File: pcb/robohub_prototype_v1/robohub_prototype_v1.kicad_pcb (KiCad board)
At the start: 10 copper layers, 102 parts, among them J21 Barrel_Jack_Switch_Pin3Ring, J51 USB_A, J52 USB_A, J71 USB_A, U1 ATSAMA5D27C, U21 LM3880, U22 TPS564242DRL, U23 TPS564242DRL, U24 TPS564242DRL, U25 TPS564242DRL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

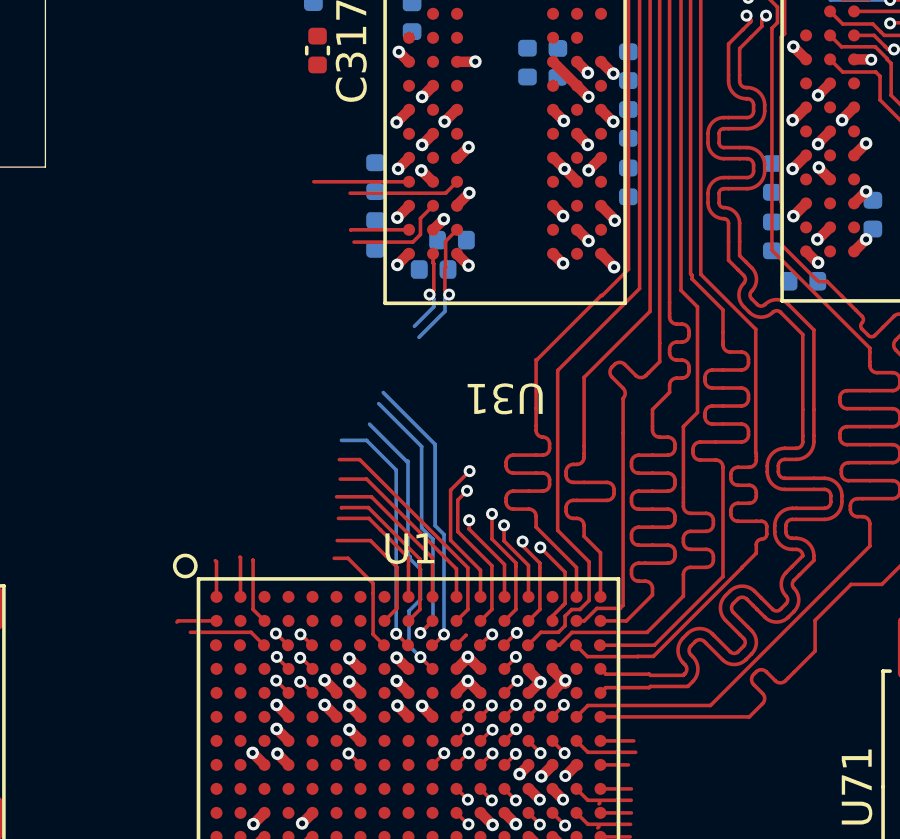
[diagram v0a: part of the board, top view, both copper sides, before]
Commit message: Routing data bytes
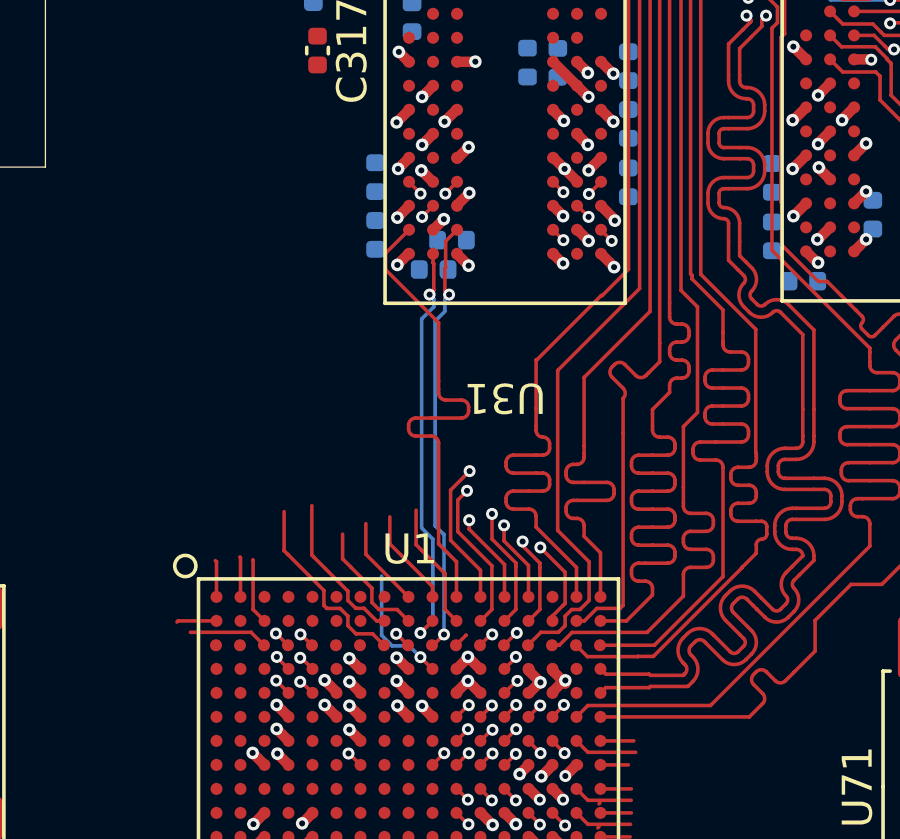
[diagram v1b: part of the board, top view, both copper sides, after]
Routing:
- net /DDR2_3/DDR_D18: track 12.0 -> 1.18 mm, vias 1 -> 2
- net /DDR2_3/DDR_D23: track 8.00 -> 16.9 mm
- net /DDR2_3/DDR_D21: track 12.5 -> 4.69 mm, vias 1 -> 2
- net /DDR2_3/DDR_DQM2: track 3.91 -> 6.90 mm, vias 0 -> 1
- net /DDR2_3/DDR_D22: track 7.73 -> 4.79 mm, vias 0 -> 1
- net /DDR2_3/DDR_D16: track 7.78 -> 5.68 mm, vias 0 -> 1
- net /DDR2_3/DDR_DQS2-: track 12.0 -> 13.9 mm
- net /DDR2_3/DDR_D20: track 5.34 -> 3.83 mm, vias 0 -> 1
- net /DDR2_3/DDR_DQS2+: track 13.7 -> 14.6 mm
- net /DDR2_3/DDR_D17: track 5.58 -> 4.73 mm, vias 0 -> 1
- net /DDR2_3/DDR_D19: track 4.18 -> 3.52 mm, vias 0 -> 1

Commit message: Updates to routing second byte lane
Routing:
- net /DDR2_3/DDR_D18: track 1.18 -> 18.6 mm
- net /DDR2_3/DDR_D16: track 5.68 -> 21.9 mm, vias 1 -> 0
- net /DDR2_3/DDR_D19: track 3.52 -> 18.9 mm
- net /DDR2_3/DDR_D21: track 4.69 -> 19.6 mm
- net /DDR2_3/DDR_D20: track 3.83 -> 18.5 mm, vias 1 -> 2
- net /DDR2_3/DDR_D17: track 4.73 -> 19.3 mm, vias 1 -> 2
- net /DDR2_3/DDR_D22: track 4.79 -> 18.0 mm, vias 1 -> 2
- net /DDR2_3/DDR_DQM2: track 6.90 -> 19.8 mm, vias 1 -> 2
- net /DDR2_3/DDR_RAS: track 37.2 -> 48.9 mm
- net /DDR2_3/DDR_WE: track 43.1 -> 49.5 mm
- net /DDR2_3/DDR_CS: track 41.6 -> 47.8 mm
- net /DDR2_3/DDR_D5: track 0.61 -> 6.42 mm, vias 1 -> 2
- net /DDR2_3/DDR_D2: track 0.61 -> 5.13 mm, vias 1 -> 2
- net /DDR2_3/DDR_A6: track 45.9 -> 49.8 mm
- net /DDR2_3/DDR_DQS2+: track 14.6 -> 18.4 mm
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
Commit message: Rip up to begin reroute
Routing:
- net /DDR2_3/DDR_A11: track 55.9 -> 3.94 mm, vias 2 -> 1
- net /DDR2_3/DDR_CKE: track 56.4 -> 7.86 mm, vias 2 -> 1
- net /DDR2_3/DDR_CLK-: track 55.8 -> 7.91 mm, vias 2 -> 1
- net /DDR2_3/DDR_BA2: track 56.5 -> 8.78 mm, vias 2 -> 1
- net /DDR2_3/DDR_CLK+: track 55.2 -> 7.63 mm, vias 2 -> 1
- net /DDR2_3/DDR_A2: track 49.6 -> 3.30 mm, vias 2 -> 1
- net /DDR2_3/DDR_A7: track 56.3 -> 10.6 mm, vias 2 -> 1
- net /DDR2_3/DDR_A4: track 50.8 -> 6.43 mm, vias 2 -> 1
- net /DDR2_3/DDR_A1: track 48.2 -> 4.70 mm, vias 2 -> 1
- net /DDR2_3/DDR_A12: track 49.3 -> 5.79 mm, vias 2 -> 1
- net /DDR2_3/DDR_A13: track 56.0 -> 13.9 mm, vias 3 -> 2
- net /DDR2_3/DDR_A3: track 49.4 -> 7.28 mm, vias 2 -> 1
- net /DDR2_3/DDR_A8: track 50.9 -> 8.91 mm, vias 2 -> 1
- net /DDR2_3/DDR_A10: track 49.1 -> 7.36 mm, vias 2 -> 1
- net /DDR2_3/DDR_CAS: track 51.0 -> 10.4 mm, vias 3 -> 2
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
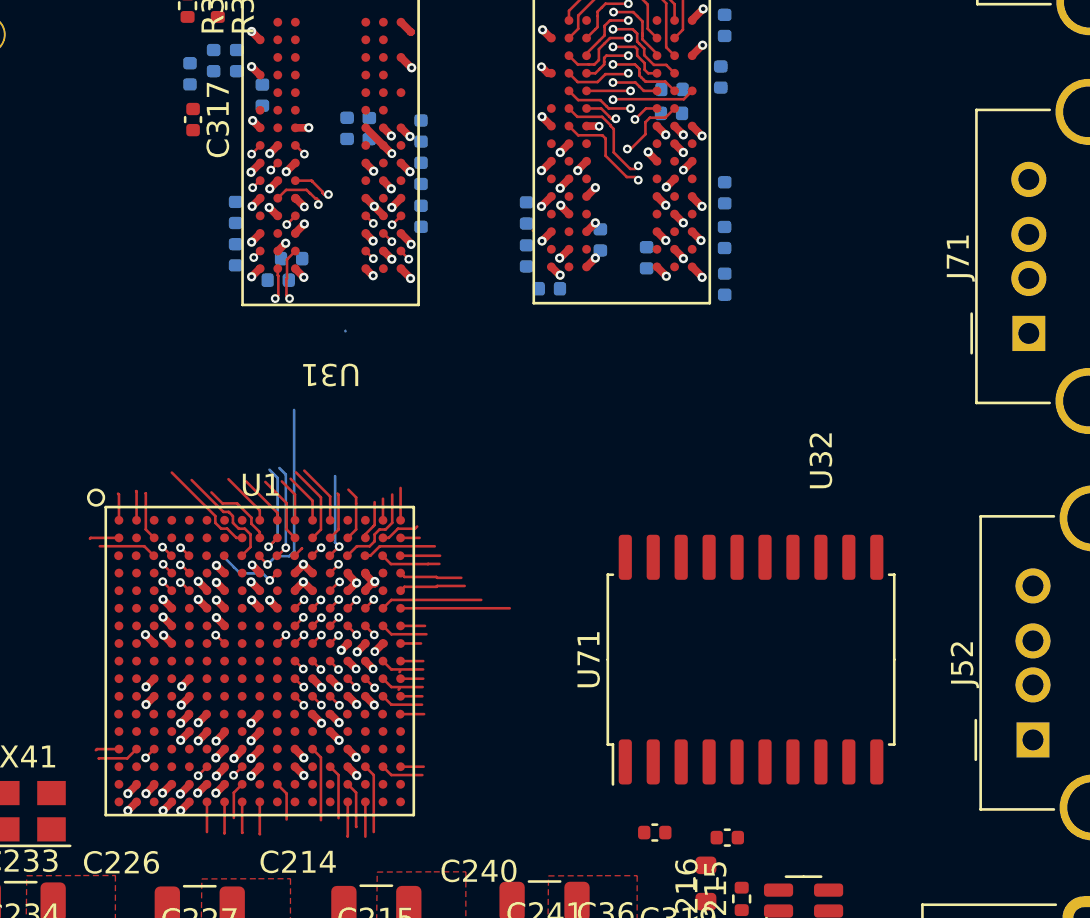
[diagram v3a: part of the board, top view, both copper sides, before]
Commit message: Routed 3/4 data bytes, no length matching
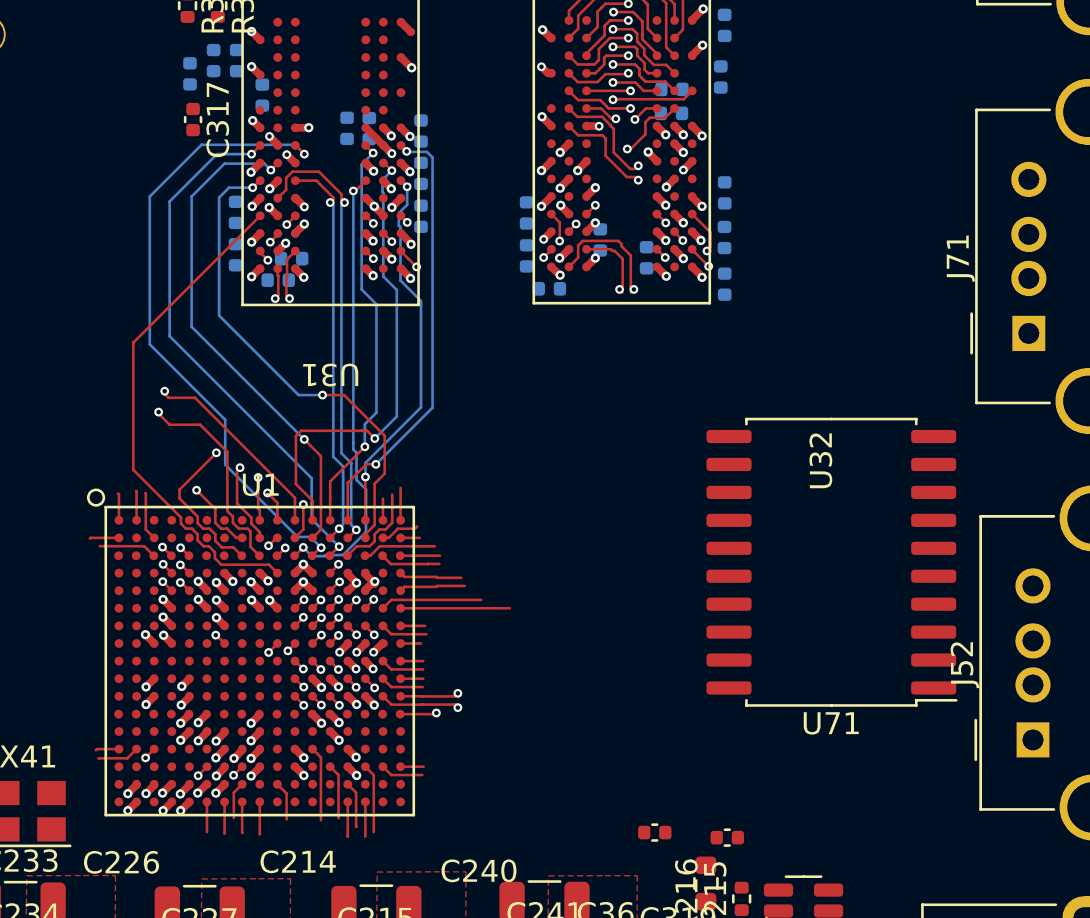
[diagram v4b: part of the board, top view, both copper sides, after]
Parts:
- moved U71 5.74 mm to (147.8, 90.2), turned to 180 degrees
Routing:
- net /DDR2_3/DDR_D27: track 0.58 -> 45.9 mm, vias 1 -> 2
- net /DDR2_3/DDR_D30: track 0.59 -> 38.9 mm, vias 1 -> 2
- net /DDR2_3/DDR_D28: track 0.66 -> 38.6 mm, vias 1 -> 2
- net /DDR2_3/DDR_D25: track 0.55 -> 37.7 mm, vias 1 -> 2
- net /DDR2_3/DDR_DQM3: track 0.69 -> 34.7 mm, vias 1 -> 2
- net /DDR2_3/DDR_DQS3-: track 1.93 -> 35.4 mm, vias 0 -> 2
- net /DDR2_3/DDR_D29: track 0.63 -> 33.8 mm, vias 1 -> 2
- net /DDR2_3/DDR_D26: track 0.53 -> 32.8 mm, vias 1 -> 2
- net /DDR2_3/DDR_D24: track 0.54 -> 32.0 mm, vias 1 -> 2
- net /DDR2_3/DDR_DQS3+: track 0.99 -> 31.5 mm, vias 0 -> 2
- net /DDR2_3/DDR_D31: track 1.09 -> 29.0 mm, vias 0 -> 2
- net /DDR2_3/DDR_D2: track 5.13 -> 29.5 mm
- net /DDR2_3/DDR_DQM0: track 0.47 -> 20.5 mm, vias 0 -> 2
- net /DDR2_3/DDR_D4: track 0.00 -> 20.0 mm, vias 0 -> 2
- net /DDR2_3/DDR_D21: track 2.97 -> 23.0 mm, vias 1 -> 0
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
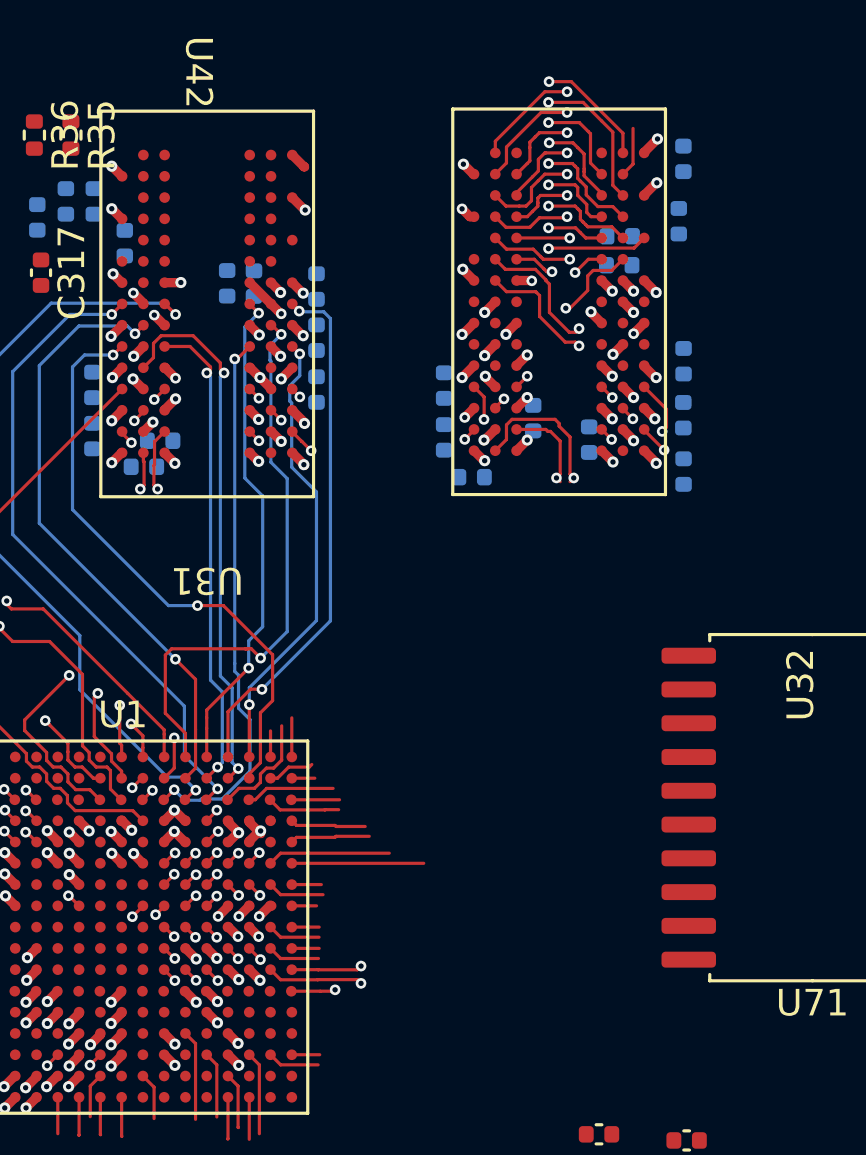
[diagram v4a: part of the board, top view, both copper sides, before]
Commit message: Routing data byte groups and half of address
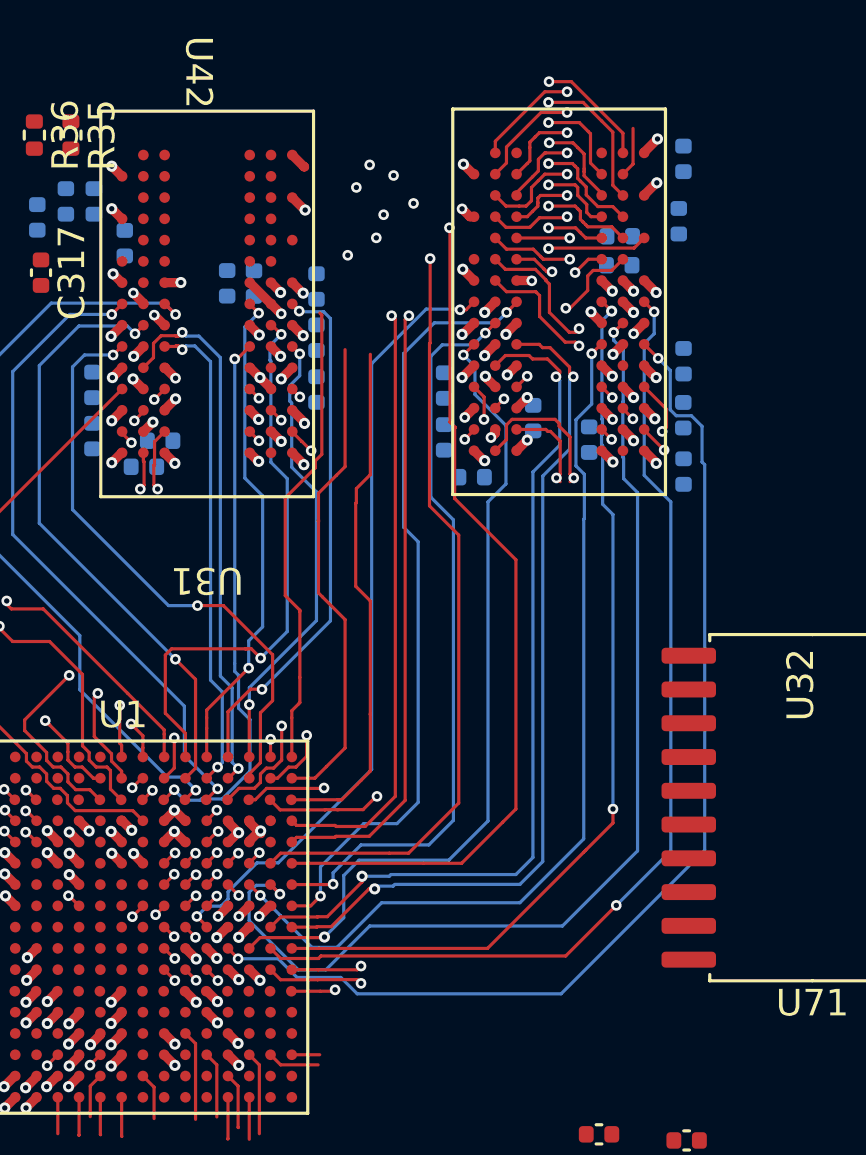
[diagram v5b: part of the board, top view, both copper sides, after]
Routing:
- net /DDR2_3/DDR_D14: track 0.57 -> 41.2 mm, vias 1 -> 2
- net /DDR2_3/DDR_D9: track 2.13 -> 40.6 mm, vias 0 -> 2
- net /DDR2_3/DDR_D12: track 1.96 -> 38.3 mm, vias 0 -> 2
- net /DDR2_3/DDR_DQM1: track 0.58 -> 34.4 mm, vias 1 -> 2
- net /DDR2_3/DDR_D11: track 1.03 -> 34.2 mm, vias 0 -> 2
- net /DDR2_3/DDR_BA2: track 8.74 -> 40.0 mm, vias 1 -> 2
- net /DDR2_3/DDR_CAS: track 12.6 -> 43.9 mm, vias 2 -> 3
- net /DDR2_3/DDR_DQS1+: track 1.03 -> 31.9 mm, vias 0 -> 2
- net /DDR2_3/DDR_DQS1-: track 1.98 -> 32.7 mm, vias 0 -> 2
- net /DDR2_3/DDR_CKE: track 7.86 -> 38.3 mm, vias 1 -> 2
- net /DDR2_3/DDR_D15: track 0.62 -> 30.9 mm, vias 1 -> 2
- net /DDR2_3/DDR_CS: track 10.9 -> 40.7 mm, vias 2 -> 3
- net /DDR2_3/DDR_D13: track 0.54 -> 29.7 mm, vias 1 -> 2
- net /DDR2_3/DDR_A0: track 13.0 -> 41.8 mm, vias 2 -> 3
- net /DDR2_3/DDR_BA1: track 13.3 -> 41.8 mm, vias 2 -> 3
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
